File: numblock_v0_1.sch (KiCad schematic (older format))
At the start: 46 parts, among them J1 Conn_01x14_Female, J2 Conn_01x14_Female, J3 Conn_01x05_Female, J4 Conn_02x03_Odd_Even, J5 Conn_01x03_Female, SW1 SW_PUSH-MX_W_LED, SW10 SW_PUSH-MX_W_LED, SW11 SW_PUSH-MX_W_LED, SW12 SW_PUSH-MX_W_LED, SW13 SW_PUSH-MX_W_LED, SW14 SW_PUSH-MX_W_LED, SW15 SW_PUSH-MX_W_LED, SW16 SW_PUSH-MX_W_LED, SW17 SW_PUSH-MX_W_LED, SW18 SW_PUSH-MX_W_LED, SW19 SW_PUSH-MX_W_LED, SW2 SW_PUSH-MX_W_LED, SW20 SW_PUSH-MX_W_LED, SW21 Rotary_Encoder_Switch, SW3 SW_PUSH-MX_W_LED, SW4 SW_PUSH-MX_W_LED, SW5 SW_PUSH-MX_W_LED, SW6 SW_PUSH-MX_W_LED, SW7 SW_PUSH-MX_W_LED, SW8 SW_PUSH-MX_W_LED, SW9 SW_PUSH-MX_W_LED

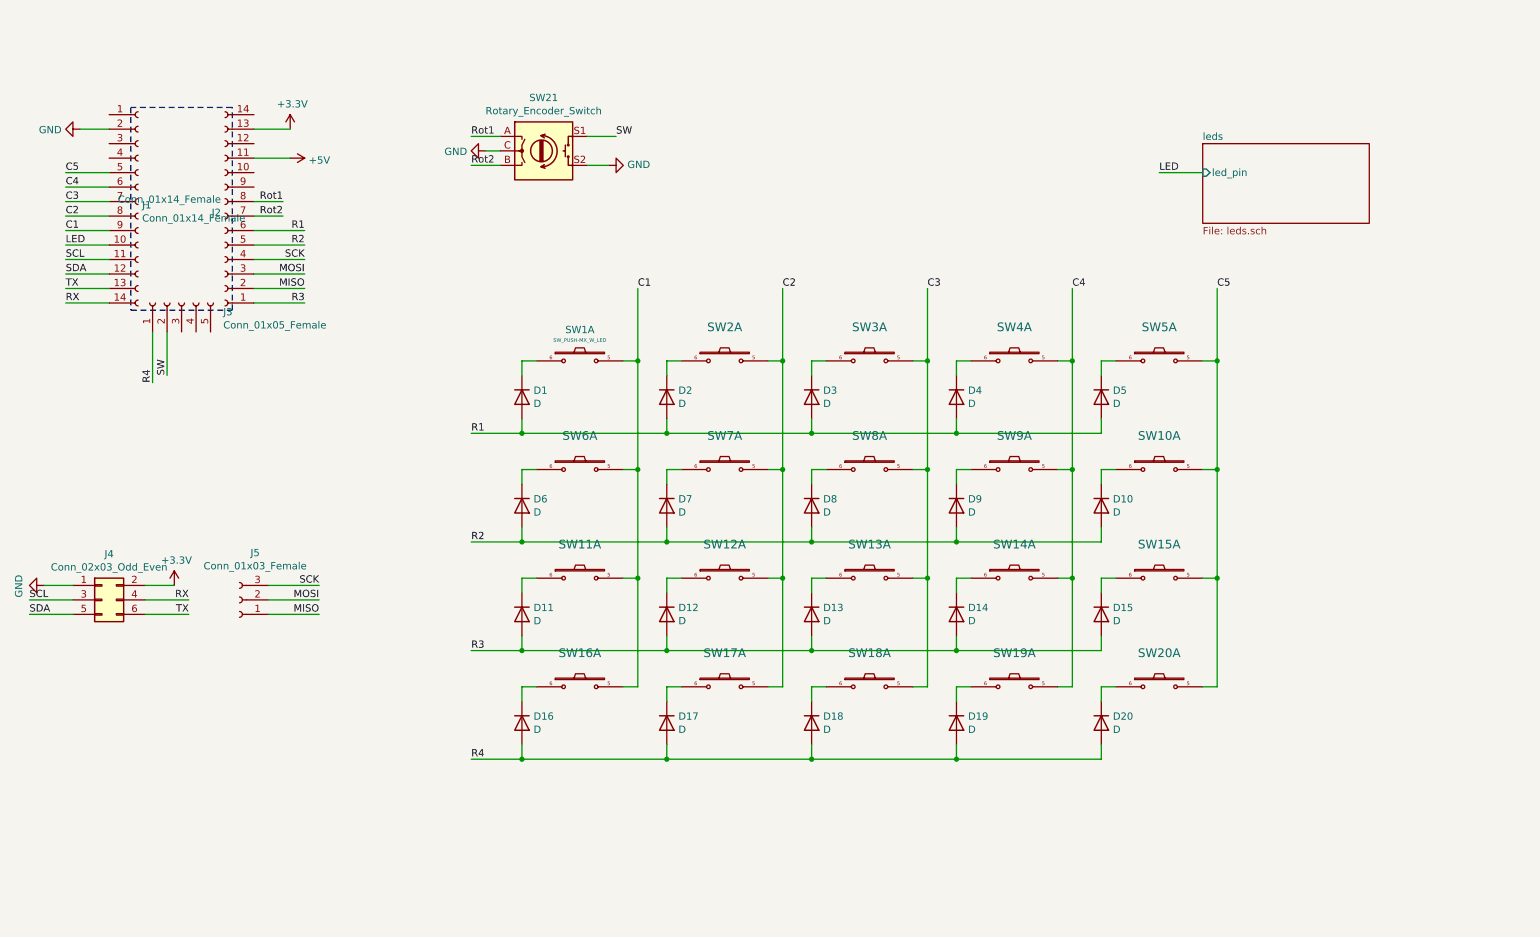
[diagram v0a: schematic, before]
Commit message: kinda done, about to add jumpers for rot. enc.
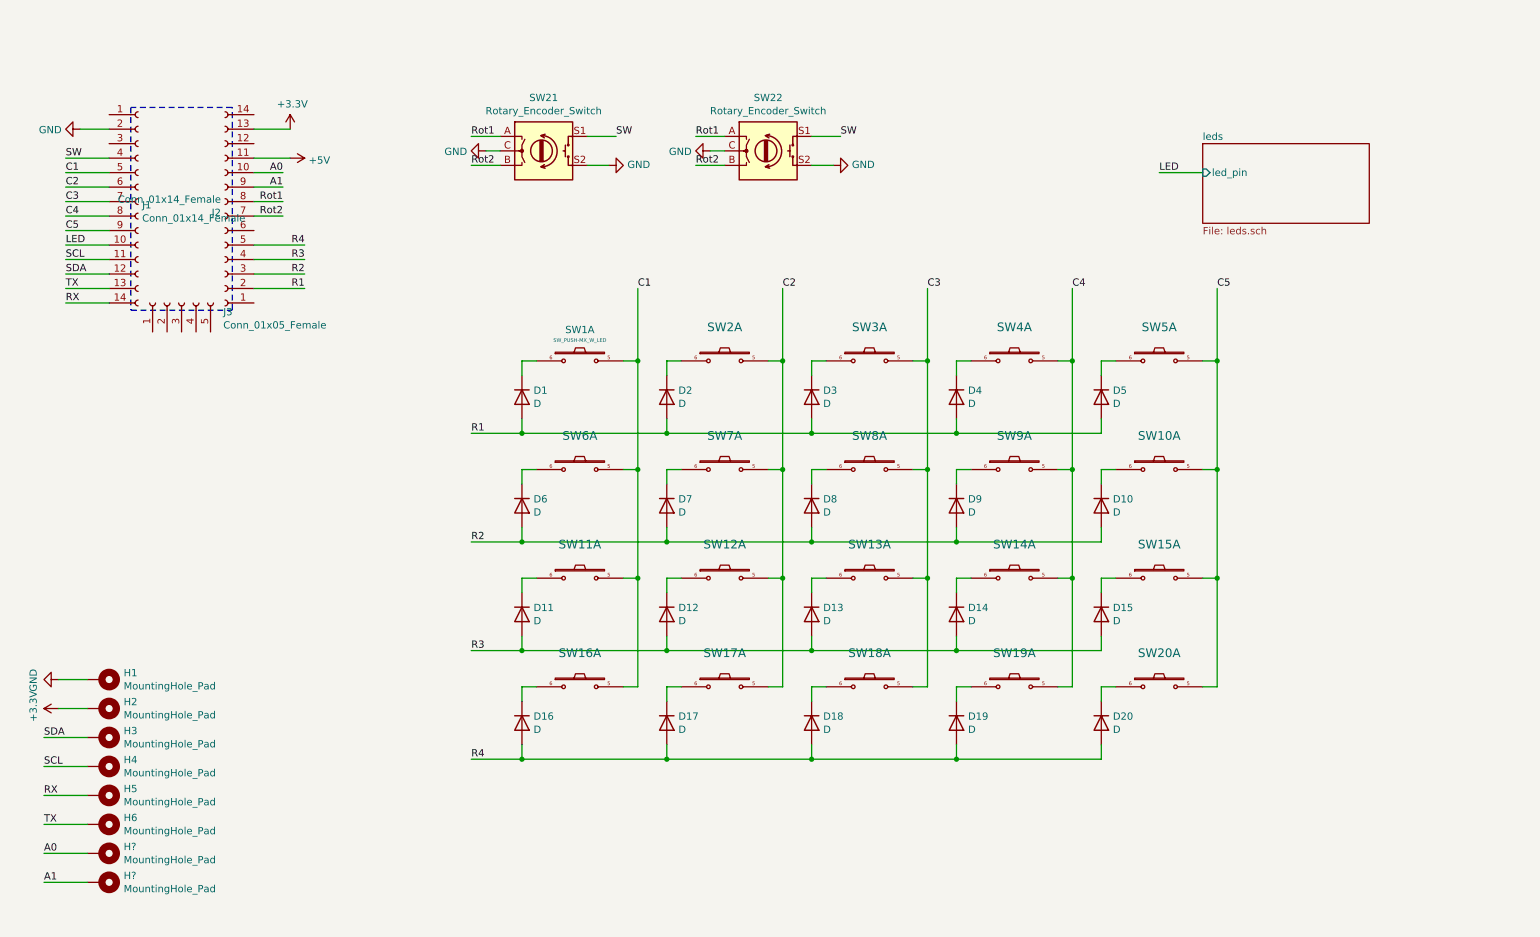
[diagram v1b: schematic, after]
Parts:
- removed J4: Conn_02x03_Odd_Even, Connector_PinSocket_2.54mm:PinSocket_2x03_P2.54mm_Vertical, symbol Connector_Generic:Conn_02x03_Odd_Even
- removed J5: Conn_01x03_Female, Connector_PinSocket_2.54mm:PinSocket_1x03_P2.54mm_Vertical, symbol Connector:Conn_01x03_Female
- added H1, H2, H3, H4, H5, H6, H? (x2): MountingHole_Pad, sofle RGB:hole_30mil, symbol Mechanical:MountingHole_Pad
- added SW22: Rotary_Encoder_Switch, sofle RGB:RotaryEncoder_Alps_EC11E-Switch_Vertical_H20mm_NoMountingHoles, symbol Device:Rotary_Encoder_Switch
- SW21: footprint Rotary_Encoder:RotaryEncoder_Alps_EC11E-Switch_Vertical_H20mm_CircularMountingHoles -> sofle RGB:RotaryEncoder_Alps_EC11E-Switch_Vertical_H20mm_NoMountingHoles
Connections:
- net MISO is gone; now on net R1: J2.2 (Pin_2)
- net MOSI is gone; now on net R2: J2.3 (Pin_3)
- net SCK is gone; now on net R3: J2.4 (Pin_4)
- net +3V3: now also H2.1
- net C1: now also J1.5 (Pin_5); no longer J1.9 (Pin_9)
- net C2: now also J1.6 (Pin_6); no longer J1.8 (Pin_8)
- net C4: now also J1.8 (Pin_8); no longer J1.6 (Pin_6)
- net C5: now also J1.9 (Pin_9); no longer J1.5 (Pin_5)
- net GND: now also H1.1, SW22.C, SW22.S2
- net R1: no longer J2.6 (Pin_6)
- net R2: no longer J2.5 (Pin_5)
- net R3: no longer J2.1 (Pin_1)
- net R4: now also J2.5 (Pin_5); no longer J3.1 (Pin_1)
- net RX: now also H5.1
- net Rot1: now also SW22.A
- net Rot2: now also SW22.B
- net SCL: now also H4.1
- net SDA: now also H3.1
- net SW: now also J1.4 (Pin_4), SW22.S1; no longer J3.2 (Pin_2)
- net TX: now also H6.1
- net A0: now reaches J2.10 (Pin_10)
- net A0: now also H?.1
- net A1: now reaches J2.9 (Pin_9)
- net A1: now also H?.1
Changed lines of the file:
@@
 F 0 "SW21" H 4350 1917 50  0000 C CNN
 F 1 "Rotary_Encoder_Switch" H 4350 1826 50  0000 C CNN
-F 2 "Rotary_Encoder:RotaryEncoder_Alps_EC11E-Switch_Vertical_H20mm_CircularMountingHoles" H 4200 1710 50  0001 C CNN
+F 2 "sofle RGB:RotaryEncoder_Alps_EC11E-Switch_Vertical_H20mm_NoMountingHoles" H 4200 1710 50  0001 C CNN
 F 3 "~" H 4350 1810 50  0001 C CNN
 	1    4350 1550
@@
 Wire Wire Line
 	5000 3000 4900 3000
-Text Label 2700 2100 2    50   ~ 0
+Text Label 2700 2200 2    50   ~ 0
+R4
+Text Label 2700 2300 2    50   ~ 0
+R3
+Text Label 2700 2400 2    50   ~ 0
+R2
+Text Label 2700 2500 2    50   ~ 0
 R1
-Text Label 2700 2200 2    50   ~ 0
-R2
-Text Label 2700 2600 2    50   ~ 0
-R3
-Text Label 1650 3150 1    50   ~ 0
-R4
 Text Label 5000 2500 0    50   ~ 0
 C1
@@
 C4
 Wire Wire Line
-	2700 2100 2350 2100
-Wire Wire Line
 	2700 2200 2350 2200
 Wire Wire Line
-	2700 2600 2350 2600
-Wire Wire Line
-	1650 3150 1650 2800
+	2700 2300 2350 2300
+Wire Wire Line
+	2700 2400 2350 2400
+Wire Wire Line
+	2700 2500 2350 2500
 Wire Wire Line
 	1050 1700 1350 1700
@@
 Connection ~ 8000 3000
 Text Label 1050 2100 0    50   ~ 0
-C1
+C5
 Wire Wire Line
 	1050 2100 1350 2100
 Text Label 1050 2000 0    50   ~ 0
-C2
+C4
 Wire Wire Line
 	1050 2000 1350 2000
@@
 	1050 1900 1350 1900
 Text Label 1050 1800 0    50   ~ 0
-C4
+C2
 Wire Wire Line
 	4650 1450 4850 1450
@@
 SW
 Wire Wire Line
-	1750 2800 1750 3100
-Text Label 1750 3100 1    50   ~ 0
+	1350 1600 1050 1600
+Text Label 1050 1600 0    50   ~ 0
 SW
 Text Label 3850 1450 0    50   ~ 0
@@
 Wire Wire Line
 	1350 2600 1050 2600
-Text Label 1900 4650 2    50   ~ 0
+Text Label 900  6000 0    50   ~ 0
 RX
-Text Label 1900 4750 2    50   ~ 0
+Text Label 900  6200 0    50   ~ 0
 TX
-Text Label 800  4750 0    50   ~ 0
+Text Label 900  5600 0    50   ~ 0
 SDA
-Text Label 800  4650 0    50   ~ 0
+Text Label 900  5800 0    50   ~ 0
 SCL
 Wire Wire Line
-	1100 4650 800  4650
-Wire Wire Line
-	800  4750 1100 4750
-Wire Wire Line
-	1600 4750 1900 4750
-Wire Wire Line
-	1600 4650 1900 4650
+	1200 5800 900  5800
+Wire Wire Line
+	900  5600 1200 5600
+Wire Wire Line
+	1200 6200 900  6200
+Wire Wire Line
+	1200 6000 900  6000
 $Comp
 L power:GND #PWR05
 U 1 1 60A26A05
-P 900 4550
-F 0 "#PWR05" H 900 4300 50  0001 C CNN
-F 1 "GND" H 905 4377 50  0000 C CNN
-F 2 "" H 900 4550 50  0001 C CNN
-F 3 "" H 900 4550 50  0001 C CNN
-	1    900  4550
-	0    1    1    0
-$EndComp
-Wire Wire Line
-	1100 4550 900  4550
-Wire Wire Line
-	1600 4550 1800 4550
+P 1000 5200
+F 0 "#PWR05" H 1000 4950 50  0001 C CNN
+F 1 "GND" H 1005 5027 50  0000 C CNN
+F 2 "" H 1000 5200 50  0001 C CNN
+F 3 "" H 1000 5200 50  0001 C CNN
+	1    1000 5200
+	0    1    1    0
+$EndComp
+Wire Wire Line
+	1200 5200 1000 5200
+Wire Wire Line
+	1200 5400 1000 5400
 Wire Wire Line
 	1350 2200 1050 2200
 Text Label 1050 2200 0    50   ~ 0
 LED
-$Comp
-L Connector_Generic:Conn_02x03_Odd_Even J4
-U 1 1 60976B7C
-P 1300 4650
-F 0 "J4" H 1350 4967 50  0000 C CNN
-F 1 "Conn_02x03_Odd_Even" H 1350 4876 50  0000 C CNN
-F 2 "Connector_PinSocket_2.54mm:PinSocket_2x03_P2.54mm_Vertical" H 1300 4650 50  0001 C CNN
-F 3 "~" H 1300 4650 50  0001 C CNN
-	1    1300 4650
-	1    0    0    -1
-$EndComp
 $Comp
 L sofle_rgb:SW_PUSH-MX_W_LED SW1
@@
 $EndComp
 Text Label 1050 1700 0    50   ~ 0
-C5
-Wire Wire Line
-	2350 2300 2700 2300
-Wire Wire Line
-	2350 2400 2700 2400
-Wire Wire Line
-	2350 2500 2700 2500
-Text Label 2700 2300 2    50   ~ 0
-SCK
-Text Label 2700 2400 2    50   ~ 0
-MOSI
-Text Label 2700 2500 2    50   ~ 0
-MISO
+C1
 Wire Wire Line
 	1050 1800 1350 1800
-$Comp
-L Connector:Conn_01x03_Female J5
-U 1 1 60C97DC5
-P 2250 4650
-F 0 "J5" H 2142 4325 50  0000 C CNN
-F 1 "Conn_01x03_Female" H 2142 4416 50  0000 C CNN
-F 2 "Connector_PinSocket_2.54mm:PinSocket_1x03_P2.54mm_Vertical" H 2250 4650 50  0001 C CNN
-F 3 "~" H 2250 4650 50  0001 C CNN
-	1    2250 4650
-	-1   0    0    1
-$EndComp
-Wire Wire Line
-	2450 4550 2800 4550
-Wire Wire Line
-	2450 4650 2800 4650
-Wire Wire Line
-	2450 4750 2800 4750
-Text Label 2800 4550 2    50   ~ 0
-SCK
-Text Label 2800 4650 2    50   ~ 0
-MOSI
-Text Label 2800 4750 2    50   ~ 0
-MISO
 $Comp
 L power:GND #PWR0102
@@
 L power:+3.3V #PWR0104
 U 1 1 60D547AF
-P 1800 4550
-F 0 "#PWR0104" H 1800 4400 50  0001 C CNN
-F 1 "+3.3V" H 1815 4723 50  0000 C CNN
-F 2 "" H 1800 4550 50  0001 C CNN
-F 3 "" H 1800 4550 50  0001 C CNN
-	1    1800 4550
-	1    0    0    -1
-$EndComp
+P 1000 5400
+F 0 "#PWR0104" H 1000 5250 50  0001 C CNN
+F 1 "+3.3V" H 1015 5573 50  0000 C CNN
+F 2 "" H 1000 5400 50  0001 C CNN
+F 3 "" H 1000 5400 50  0001 C CNN
+	1    1000 5400
+	0    -1   -1   0
+$EndComp
+$Comp
+L Mechanical:MountingHole_Pad H1
+U 1 1 60A6D999
+P 1300 5200
+F 0 "H1" V 1254 5350 50  0000 L CNN
+F 1 "MountingHole_Pad" V 1345 5350 50  0000 L CNN
+F 2 "sofle RGB:hole_30mil" H 1300 5200 50  0001 C CNN
+F 3 "~" H 1300 5200 50  0001 C CNN
+	1    1300 5200
+	0    1    1    0
+$EndComp
+$Comp
+L Mechanical:MountingHole_Pad H2
+U 1 1 60A6DEB5
+P 1300 5400
+F 0 "H2" V 1254 5550 50  0000 L CNN
+F 1 "MountingHole_Pad" V 1345 5550 50  0000 L CNN
+F 2 "sofle RGB:hole_30mil" H 1300 5400 50  0001 C CNN
+F 3 "~" H 1300 5400 50  0001 C CNN
+	1    1300 5400
+	0    1    1    0
+$EndComp
+$Comp
+L Mechanical:MountingHole_Pad H3
+U 1 1 60A6E1AD
+P 1300 5600
+F 0 "H3" V 1254 5750 50  0000 L CNN
+F 1 "MountingHole_Pad" V 1345 5750 50  0000 L CNN
+F 2 "sofle RGB:hole_30mil" H 1300 5600 50  0001 C CNN
+F 3 "~" H 1300 5600 50  0001 C CNN
+	1    1300 5600
+	0    1    1    0
+$EndComp
+$Comp
+L Mechanical:MountingHole_Pad H4
+U 1 1 60A70C0B
+P 1300 5800
+F 0 "H4" V 1254 5950 50  0000 L CNN
+F 1 "MountingHole_Pad" V 1345 5950 50  0000 L CNN
+F 2 "sofle RGB:hole_30mil" H 1300 5800 50  0001 C CNN
+F 3 "~" H 1300 5800 50  0001 C CNN
+	1    1300 5800
+	0    1    1    0
+$EndComp
+$Comp
+L Mechanical:MountingHole_Pad H5
+U 1 1 60A711CB
+P 1300 6000
+F 0 "H5" V 1254 6150 50  0000 L CNN
+F 1 "MountingHole_Pad" V 1345 6150 50  0000 L CNN
+F 2 "sofle RGB:hole_30mil" H 1300 6000 50  0001 C CNN
+F 3 "~" H 1300 6000 50  0001 C CNN
+	1    1300 6000
+	0    1    1    0
+$EndComp
+$Comp
+L Mechanical:MountingHole_Pad H6
+U 1 1 60A711D5
+P 1300 6200
+F 0 "H6" V 1254 6350 50  0000 L CNN
+F 1 "MountingHole_Pad" V 1345 6350 50  0000 L CNN
+F 2 "sofle RGB:hole_30mil" H 1300 6200 50  0001 C CNN
+F 3 "~" H 1300 6200 50  0001 C CNN
+	1    1300 6200
+	0    1    1    0
+$EndComp
+$Comp
+L Device:Rotary_Encoder_Switch SW22
+U 1 1 609EC679
+P 5900 1550
+F 0 "SW22" H 5900 1917 50  0000 C CNN
+F 1 "Rotary_Encoder_Switch" H 5900 1826 50  0000 C CNN
+F 2 "sofle RGB:RotaryEncoder_Alps_EC11E-Switch_Vertical_H20mm_NoMountingHoles" H 5750 1710 50  0001 C CNN
+F 3 "~" H 5900 1810 50  0001 C CNN
+	1    5900 1550
+	1    0    0    -1
+$EndComp
+Wire Wire Line
+	6200 1450 6400 1450
+Text Label 6400 1450 0    50   ~ 0
+SW
+Text Label 5400 1450 0    50   ~ 0
+Rot1
+Text Label 5400 1650 0    50   ~ 0
+Rot2
+Wire Wire Line
+	5400 1650 5600 1650
+Wire Wire Line
+	5600 1450 5400 1450
+$Comp
+L power:GND #PWR0105
+U 1 1 609ECC55
+P 6350 1650
+F 0 "#PWR0105" H 6350 1400 50  0001 C CNN
+F 1 "GND" V 6355 1522 50  0000 R CNN
+F 2 "" H 6350 1650 50  0001 C CNN
+F 3 "" H 6350 1650 50  0001 C CNN
+	1    6350 1650
+	0    -1   -1   0
+$EndComp
+Wire Wire Line
+	6350 1650 6200 1650
+$Comp
+L power:GND #PWR0106
+U 1 1 609ECC60
+P 5500 1550
+F 0 "#PWR0106" H 5500 1300 50  0001 C CNN
+F 1 "GND" V 5505 1422 50  0000 R CNN
+F 2 "" H 5500 1550 50  0001 C CNN
+F 3 "" H 5500 1550 50  0001 C CNN
+	1    5500 1550
+	0    1    1    0
+$EndComp
+Wire Wire Line
+	5500 1550 5600 1550
+Text Label 900  6400 0    50   ~ 0
+A0
+Text Label 900  6600 0    50   ~ 0
+A1
+Wire Wire Line
+	1200 6600 900  6600
+Wire Wire Line
+	1200 6400 900  6400
+$Comp
+L Mechanical:MountingHole_Pad H?
+U 1 1 60A6EC20
+P 1300 6400
+F 0 "H?" V 1254 6550 50  0000 L CNN
+F 1 "MountingHole_Pad" V 1345 6550 50  0000 L CNN
+F 2 "sofle RGB:hole_30mil" H 1300 6400 50  0001 C CNN
+F 3 "~" H 1300 6400 50  0001 C CNN
+	1    1300 6400
+	0    1    1    0
+$EndComp
+$Comp
+L Mechanical:MountingHole_Pad H?
+U 1 1 60A6EC2A
+P 1300 6600
+F 0 "H?" V 1254 6750 50  0000 L CNN
+F 1 "MountingHole_Pad" V 1345 6750 50  0000 L CNN
+F 2 "sofle RGB:hole_30mil" H 1300 6600 50  0001 C CNN
+F 3 "~" H 1300 6600 50  0001 C CNN
+	1    1300 6600
+	0    1    1    0
+$EndComp
+Text Label 2550 1700 2    50   ~ 0
+A0
+Text Label 2550 1800 2    50   ~ 0
+A1
+Wire Wire Line
+	2550 1800 2350 1800
+Wire Wire Line
+	2350 1700 2550 1700
 $EndSCHEMATC
